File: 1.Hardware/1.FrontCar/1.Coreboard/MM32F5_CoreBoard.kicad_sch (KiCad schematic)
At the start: 68 parts, among them J1 IPS114, J2 USB-Type-C, J3 BTB_02x30, J4 BTB_02x30, J5 SH1.0_4P, J6 SH1.0_2P, J7 SH1.0_2P, SW1 3x4, SW2 3x4, SW3 3x4, SW4 3x4, U1 RT9013-33GB, U2 CH343P, U3 SN65HVD232, U4 SN65HVD232, U5 MM32F5277E9P, U6 MPU-6050, Y1 32.768KHz, Y2 8MHz

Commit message: 细调
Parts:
- C30: footprint ErBW_s:C_0402 -> Capacitor_SMD:C_0603_1608Metric
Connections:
- net +5VA: now also J3.10 (Pin_10), J3.12 (Pin_12), J3.14 (Pin_14), J3.2 (Pin_2), J3.4 (Pin_4), J3.6 (Pin_6), J3.8 (Pin_8); no longer J3.47 (Pin_47), J3.49 (Pin_49), J3.51 (Pin_51), J3.53 (Pin_53), J3.55 (Pin_55), J3.57 (Pin_57), J3.59 (Pin_59)
- net 1DIR: now also J4.53 (Pin_53); no longer J4.20 (Pin_20)
- net 1LSB: now also J3.23 (Pin_23); no longer J3.20 (Pin_20)
- net 1PWM: now also J4.51 (Pin_51); no longer J4.18 (Pin_18)
- net 2DIR: now also J4.38 (Pin_38), J4.49 (Pin_49); no longer J4.16 (Pin_16), J4.52 (Pin_52)
- net 2LSB: now also J4.36 (Pin_36); no longer J4.49 (Pin_49)
- net 2PWM: now also J4.47 (Pin_47); no longer J4.14 (Pin_14)
- net ADC_DIS: now also J3.52 (Pin_52); no longer J4.22 (Pin_22)
- net ADC_VBAT: now also J3.50 (Pin_50); no longer J4.24 (Pin_24)
- net AUX_SCL: now also J3.56 (Pin_56); no longer J3.43 (Pin_43)
- net AUX_SDA: now also J3.54 (Pin_54); no longer J3.44 (Pin_44)
- net CAM_D0: now also J4.10 (Pin_10); no longer J4.6 (Pin_6)
- net CAM_D1: now also J4.12 (Pin_12); no longer J4.5 (Pin_5)
- net CAM_D2: now also J4.14 (Pin_14); no longer J4.8 (Pin_8)
- net CAM_D3: now also J4.16 (Pin_16); no longer J4.7 (Pin_7)
- net CAM_D4: now also J4.18 (Pin_18); no longer J4.10 (Pin_10)
- net CAM_D5: now also J4.20 (Pin_20); no longer J4.9 (Pin_9)
- net CAM_D6: now also J4.22 (Pin_22); no longer J4.12 (Pin_12)
- net CAM_D7: now also J4.24 (Pin_24); no longer J4.11 (Pin_11)
- net CAM_RXD: now also J4.6 (Pin_6); no longer J4.4 (Pin_4)
- net CAM_TXD: now also J4.4 (Pin_4); no longer J4.1 (Pin_1)
- net CAM_VSYNC: now also J4.8 (Pin_8); no longer J4.3 (Pin_3)
- net CAN1_H: now also J3.60 (Pin_60); no longer J3.22 (Pin_22)
- net CAN1_L: now also J3.58 (Pin_58); no longer J3.24 (Pin_24)
- net CAN2_H: now also J3.57 (Pin_57); no longer J4.40 (Pin_40)
- net CAN2_L: now also J3.59 (Pin_59); no longer J4.38 (Pin_38)
- net ELEMAG1: now also J4.45 (Pin_45); no longer J4.13 (Pin_13)
- net ELEMAG2: now also J4.43 (Pin_43); no longer J4.15 (Pin_15)
- net ELEMAG3: now also J4.41 (Pin_41); no longer J4.17 (Pin_17)
- net ELEMAG4: now also J4.39 (Pin_39); no longer J4.19 (Pin_19)
- net ELEMAG5: now also J4.37 (Pin_37); no longer J4.21 (Pin_21)
- net ENCODER_A: now also J4.44 (Pin_44); no longer J4.53 (Pin_53)
- net ENCODER_B: now also J4.46 (Pin_46); no longer J4.56 (Pin_56)
- net GND: now also J3.1 (Pin_1), J3.11 (Pin_11), J3.13 (Pin_13), J3.15 (Pin_15), J3.3 (Pin_3), J3.5 (Pin_5), J3.7 (Pin_7), J3.9 (Pin_9); no longer J3.46 (Pin_46), J3.48 (Pin_48), J3.50 (Pin_50), J3.52 (Pin_52), J3.54 (Pin_54), J3.56 (Pin_56), J3.58 (Pin_58), J3.60 (Pin_60)
- net KEY_CENTER: now also J4.42 (Pin_42); no longer J4.54 (Pin_54)
- net MAPLE_CLK: now also J4.11 (Pin_11); no longer J4.35 (Pin_35)
- net MAPLE_CS: now also J4.13 (Pin_13); no longer J4.36 (Pin_36)
- net MAPLE_MISO: now also J4.9 (Pin_9); no longer J4.37 (Pin_37)
- net MAPLE_MOSI: now also J4.7 (Pin_7); no longer J4.39 (Pin_39)
- net PA10: now also J4.56 (Pin_56); no longer J4.59 (Pin_59)
- net PA8: now also J4.52 (Pin_52); no longer J4.57 (Pin_57)
- net PA9: now also J4.54 (Pin_54); no longer J4.60 (Pin_60)
- net PB0: now also J4.33 (Pin_33); no longer J4.26 (Pin_26)
- net PB1: now also J4.31 (Pin_31); no longer J4.25 (Pin_25)
- net PB10: now also J4.3 (Pin_3); no longer J4.41 (Pin_41)
- net PB11: now also J4.1 (Pin_1); no longer J4.44 (Pin_44)
- net PB14: now also J3.55 (Pin_55); no longer J4.43 (Pin_43)
- net PB15: now also J4.26 (Pin_26); no longer J4.46 (Pin_46)
- net PB2-BOOT1: now also J4.29 (Pin_29); no longer J4.28 (Pin_28)
- net PB3: now also J3.25 (Pin_25); no longer J3.19 (Pin_19)
- net PC10: now also J3.49 (Pin_49); no longer J3.8 (Pin_8)
- net PC11: now also J3.47 (Pin_47); no longer J3.7 (Pin_7)
- net PC13: now also J3.26 (Pin_26); no longer J3.31 (Pin_31)
- net PC5: now also J4.35 (Pin_35); no longer J4.23 (Pin_23)
- net PC8: now also J4.48 (Pin_48); no longer J4.55 (Pin_55)
- net PC9: now also J4.50 (Pin_50); no longer J4.58 (Pin_58)
- net PD0: now also J3.45 (Pin_45); no longer J3.9 (Pin_9)
- net PD1: now also J3.43 (Pin_43); no longer J3.10 (Pin_10)
- net PD10: now also J4.32 (Pin_32); no longer J4.47 (Pin_47)
- net PD11: now also J4.34 (Pin_34); no longer J4.50 (Pin_50)
- net PD15: now also J4.40 (Pin_40); no longer J4.51 (Pin_51)
- net PD3: now also J3.41 (Pin_41); no longer J3.11 (Pin_11)
- net PD8: now also J4.28 (Pin_28); no longer J4.45 (Pin_45)
- net PD9: now also J4.30 (Pin_30); no longer J4.48 (Pin_48)
- net PE0: now also J3.19 (Pin_19); no longer J3.23 (Pin_23)
- net PE1: now also J3.17 (Pin_17); no longer J3.26 (Pin_26)
- net PE10: now also J4.15 (Pin_15); no longer J4.33 (Pin_33)
- net PE15: now also J4.5 (Pin_5); no longer J4.42 (Pin_42)
- net PE2: now also J3.16 (Pin_16); no longer J3.25 (Pin_25)
- net PE3: now also J3.18 (Pin_18); no longer J3.27 (Pin_27)
- net PE4: now also J3.20 (Pin_20); no longer J3.28 (Pin_28)
- net PE9: now also J4.17 (Pin_17); no longer J4.34 (Pin_34)
- net PF0: now also J3.28 (Pin_28); no longer J3.32 (Pin_32)
- net PF1: now also J3.30 (Pin_30); no longer J3.33 (Pin_33)
- net PF10: now also J3.48 (Pin_48); no longer J3.42 (Pin_42)
- net PF12: now also J4.25 (Pin_25); no longer J4.30 (Pin_30)
- net PF13: now also J4.23 (Pin_23); no longer J4.29 (Pin_29)
- net PF14: now also J4.21 (Pin_21); no longer J4.32 (Pin_32)
- net PF15: now also J4.19 (Pin_19); no longer J4.31 (Pin_31)
- net PF2: now also J3.32 (Pin_32); no longer J3.34 (Pin_34)
- net PF3: now also J3.34 (Pin_34); no longer J3.35 (Pin_35)
- net PF5: now also J3.38 (Pin_38); no longer J3.37 (Pin_37)
- net PF6: now also J3.40 (Pin_40); no longer J3.38 (Pin_38)
- net PF7: now also J3.42 (Pin_42); no longer J3.39 (Pin_39)
- net PF8: now also J3.44 (Pin_44); no longer J3.40 (Pin_40)
- net PF9: now also J3.46 (Pin_46); no longer J3.41 (Pin_41)
- net PG10: now also J3.37 (Pin_37); no longer J3.13 (Pin_13)
- net PG11: now also J3.35 (Pin_35); no longer J3.14 (Pin_14)
- net PG12: now also J3.33 (Pin_33); no longer J3.15 (Pin_15)
- net PG13: now also J3.31 (Pin_31); no longer J3.16 (Pin_16)
- net PG14: now also J3.29 (Pin_29); no longer J3.17 (Pin_17)
- net PG15: now also J3.27 (Pin_27); no longer J3.18 (Pin_18)
- net PG9: now also J3.39 (Pin_39); no longer J3.12 (Pin_12)
- net PH2: now also J3.53 (Pin_53); no longer J3.6 (Pin_6)
- net RST: now also J4.59 (Pin_59); no longer J3.45 (Pin_45)
- net SERVO: now also J3.51 (Pin_51); no longer J3.5 (Pin_5)
- net SWCLK: now also J4.60 (Pin_60); no longer J3.1 (Pin_1)
- net SWDIO: now also J4.58 (Pin_58); no longer J3.2 (Pin_2)
- net TOF_SCL: now also J3.22 (Pin_22); no longer J3.29 (Pin_29)
- net TOF_SDA: now also J3.24 (Pin_24); no longer J3.30 (Pin_30)
- net UART1_RX: now also J4.55 (Pin_55); no longer J3.4 (Pin_4)
- net UART1_TX: now also J4.57 (Pin_57); no longer J3.3 (Pin_3)

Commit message: 信号线布局完成
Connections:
- net 1DIR: no longer J3.21 (Pin_21), U5.135 (PB5)
- net 2DIR: no longer J4.38 (Pin_38), U5.82 (PD13)
- net 1LSB renamed ENC_1LSB
- net 2LSB renamed ENC_2LSB
- new net ENC_1DIR: J3.21 (Pin_21), U5.135 (PB5)
- new net ENC_2DIR: J4.38 (Pin_38), U5.82 (PD13)
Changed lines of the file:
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@@
     (effects (font (size 1.27 1.27)) (justify left bottom))
   )
-  (label "1LSB" (at 298.45 187.96 0)
+  (label "ENC_1LSB" (at 298.45 187.96 0)
     (effects (font (size 1.27 1.27)) (justify left bottom))
   )
@@
     (effects (font (size 1.27 1.27)) (justify right bottom))
   )
-  (label "1DIR" (at 190.5 85.09 270)
+  (label "ENC_1DIR" (at 190.5 85.09 270)
     (effects (font (size 1.27 1.27)) (justify right bottom))
   )
@@
     (effects (font (size 1.27 1.27)) (justify left bottom))
   )
-  (label "1DIR" (at 298.45 185.42 0)
+  (label "ENC_1DIR" (at 298.45 185.42 0)
     (effects (font (size 1.27 1.27)) (justify left bottom))
   )
@@
     (effects (font (size 1.27 1.27)) (justify left bottom))
   )
-  (label "1LSB" (at 193.04 85.09 270)
+  (label "ENC_1LSB" (at 193.04 85.09 270)
     (effects (font (size 1.27 1.27)) (justify right bottom))
   )
@@
     (effects (font (size 1.27 1.27)) (justify right bottom))
   )
-  (label "2LSB" (at 349.25 190.5 0)
+  (label "ENC_2LSB" (at 349.25 190.5 0)
     (effects (font (size 1.27 1.27)) (justify left bottom))
   )
@@
     (effects (font (size 1.27 1.27)) (justify left bottom))
   )
-  (label "2DIR" (at 349.25 187.96 0)
+  (label "ENC_2DIR" (at 349.25 187.96 0)
     (effects (font (size 1.27 1.27)) (justify left bottom))
   )
@@
     (effects (font (size 1.27 1.27)) (justify right bottom))
   )
-  (label "2DIR" (at 279.4 171.45 180)
+  (label "ENC_2DIR" (at 279.4 171.45 180)
     (effects (font (size 1.27 1.27)) (justify right bottom))
   )
@@
     (effects (font (size 1.27 1.27)) (justify left bottom))
   )
-  (label "2LSB" (at 279.4 173.99 180)
-    (effects (font (size 1.27 1.27)) (justify right bottom))
-  )
+  (label "ENC_2LSB" (at 279.4 173.99 180)
+    (effects (font (size 1.27 1.27)) (justify right bottom))
+  )

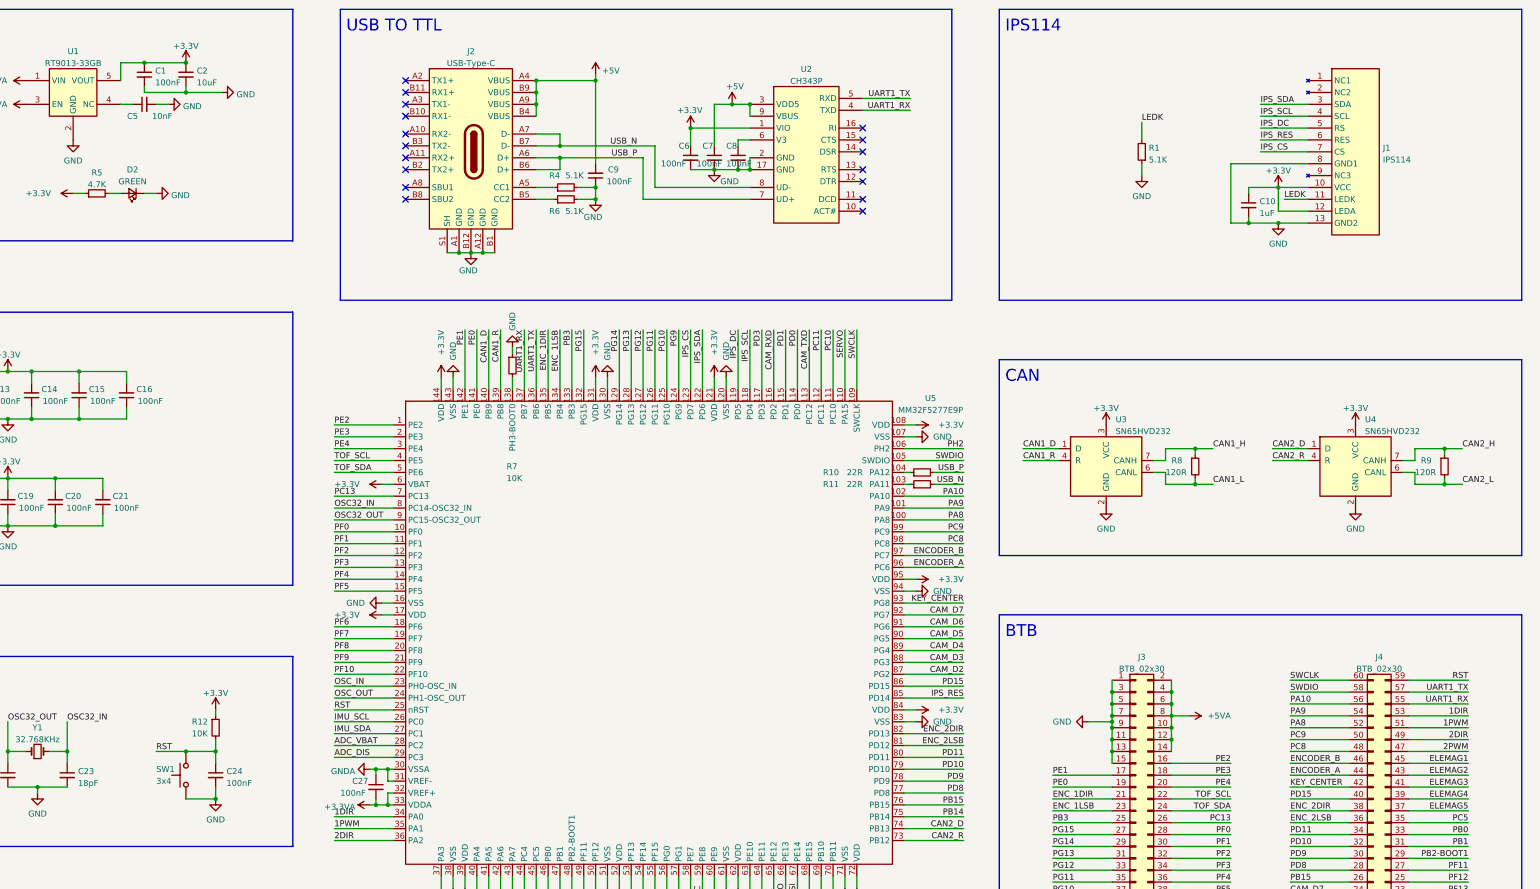
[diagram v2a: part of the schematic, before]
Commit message: 核心板v1.1，EasyUI初步实现
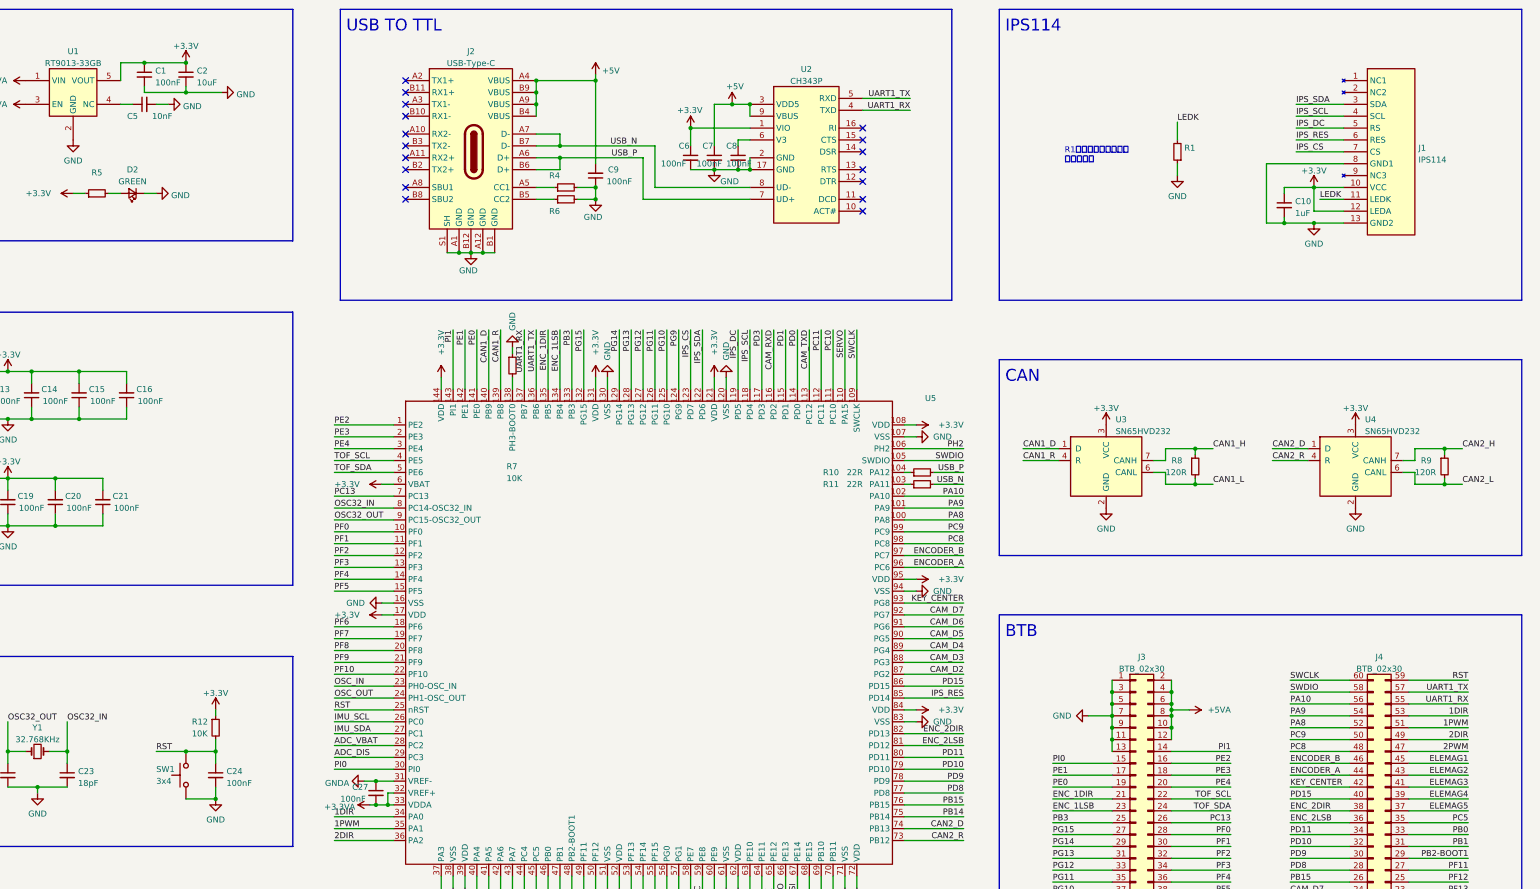
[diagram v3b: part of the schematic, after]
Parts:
- R1, R4, R6: value 5.1K -> (none)
- R5: value 4.7K -> (none)
- U5: value MM32F5277E9P -> (none)
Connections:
- net +5VA: no longer J3.14 (Pin_14)
- net GND: no longer J3.15 (Pin_15), U5.143 (VSS)
- net GNDA: no longer U5.30 (VSSA)
- new net PI0: J3.15 (Pin_15), U5.30 (PI0)
- new net PI1: J3.14 (Pin_14), U5.143 (PI1)
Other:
- note added: "R1的阻值影响背光亮度 可自由选择"
- moved on the sheet: C10, C27, J1, R1
